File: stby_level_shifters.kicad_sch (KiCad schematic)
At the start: 3 parts, among them U23 NTS0104_DHVQFN

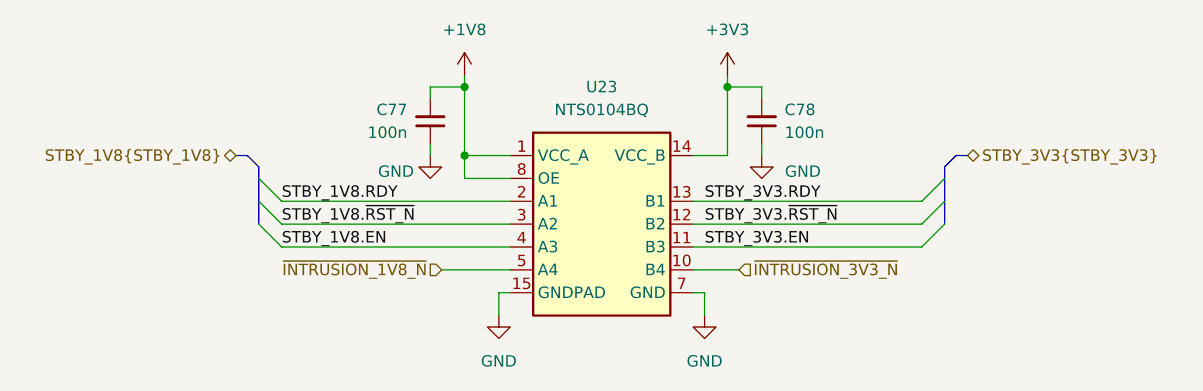
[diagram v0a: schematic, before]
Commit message: [#83148] Connect the level shifters, change STBY bus to individual signals
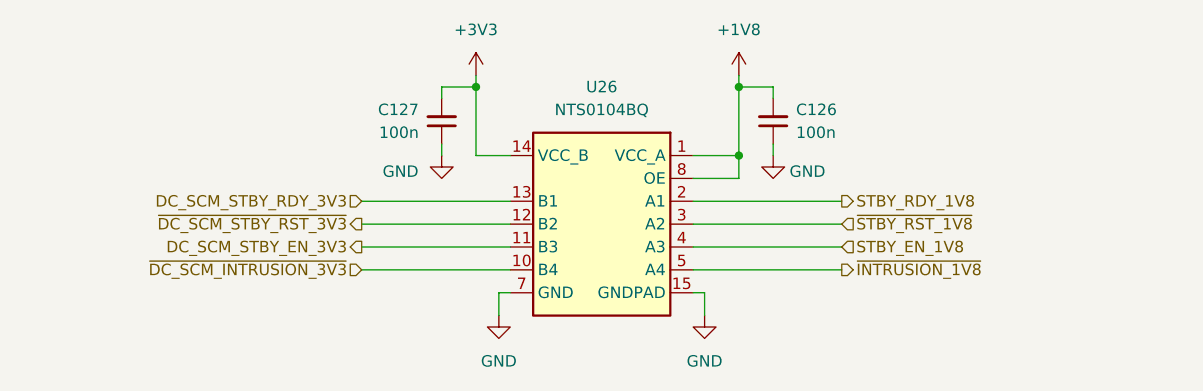
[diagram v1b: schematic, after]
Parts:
- renumbered C77 to C126, C78 to C127, U23 to U26
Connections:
- net STBY_1V8.EN renamed STBY_EN_1V8
- net STBY_1V8.RDY renamed STBY_RDY_1V8
- net STBY_1V8.~{RST_N} renamed ~{STBY_RST_1V8}
- net STBY_3V3.EN renamed DC_SCM_STBY_EN_3V3
- net STBY_3V3.RDY renamed DC_SCM_STBY_RDY_3V3
- net STBY_3V3.~{RST_N} renamed ~{DC_SCM_STBY_RST_3V3}
- net ~{INTRUSION_1V8_N} renamed ~{INTRUSION_1V8}
- net ~{INTRUSION_3V3_N} renamed ~{DC_SCM_INTRUSION_3V3}
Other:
- moved on the sheet: C126, C127

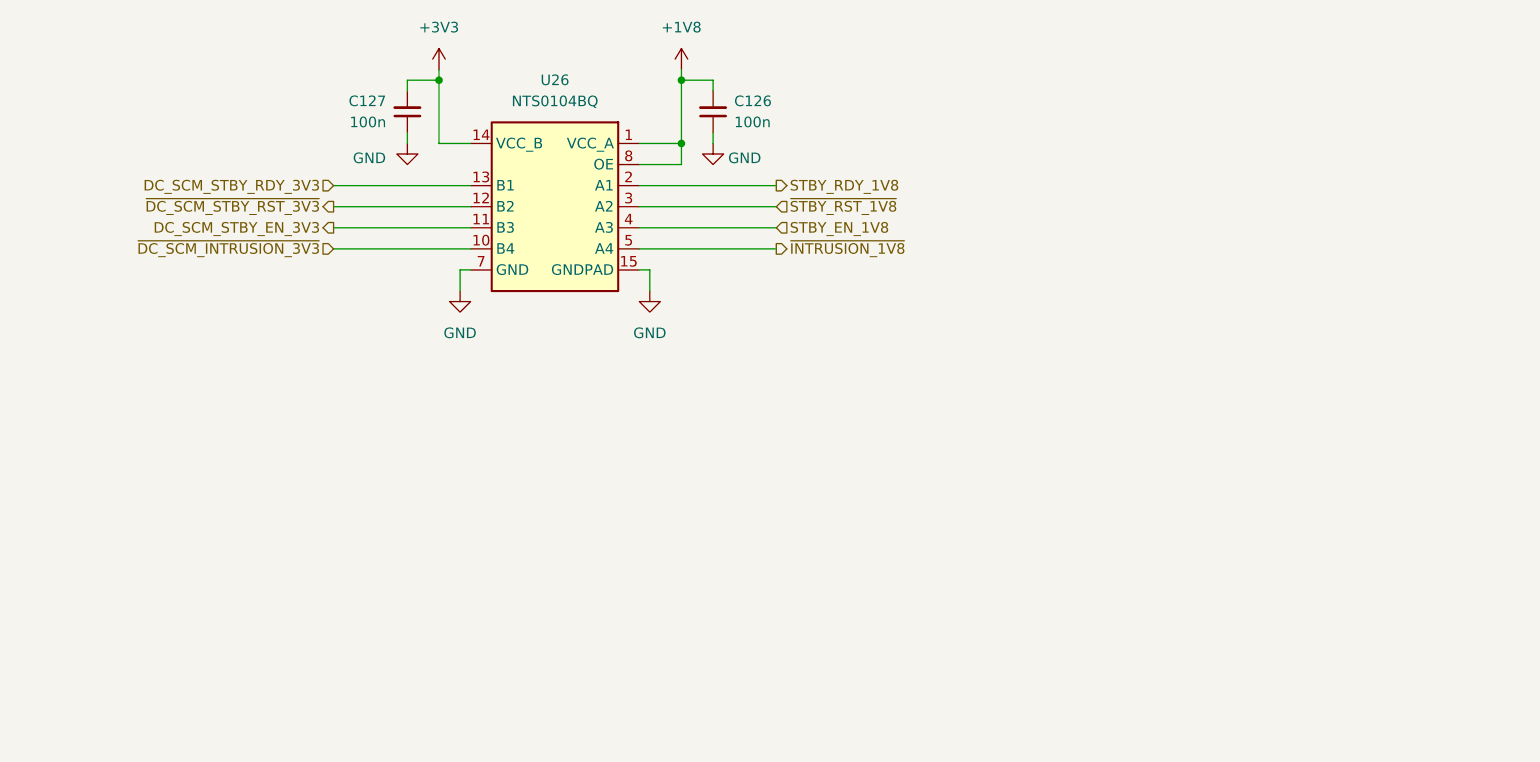
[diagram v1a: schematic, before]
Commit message: Changed A4 sheets to A3 and cleaned them up
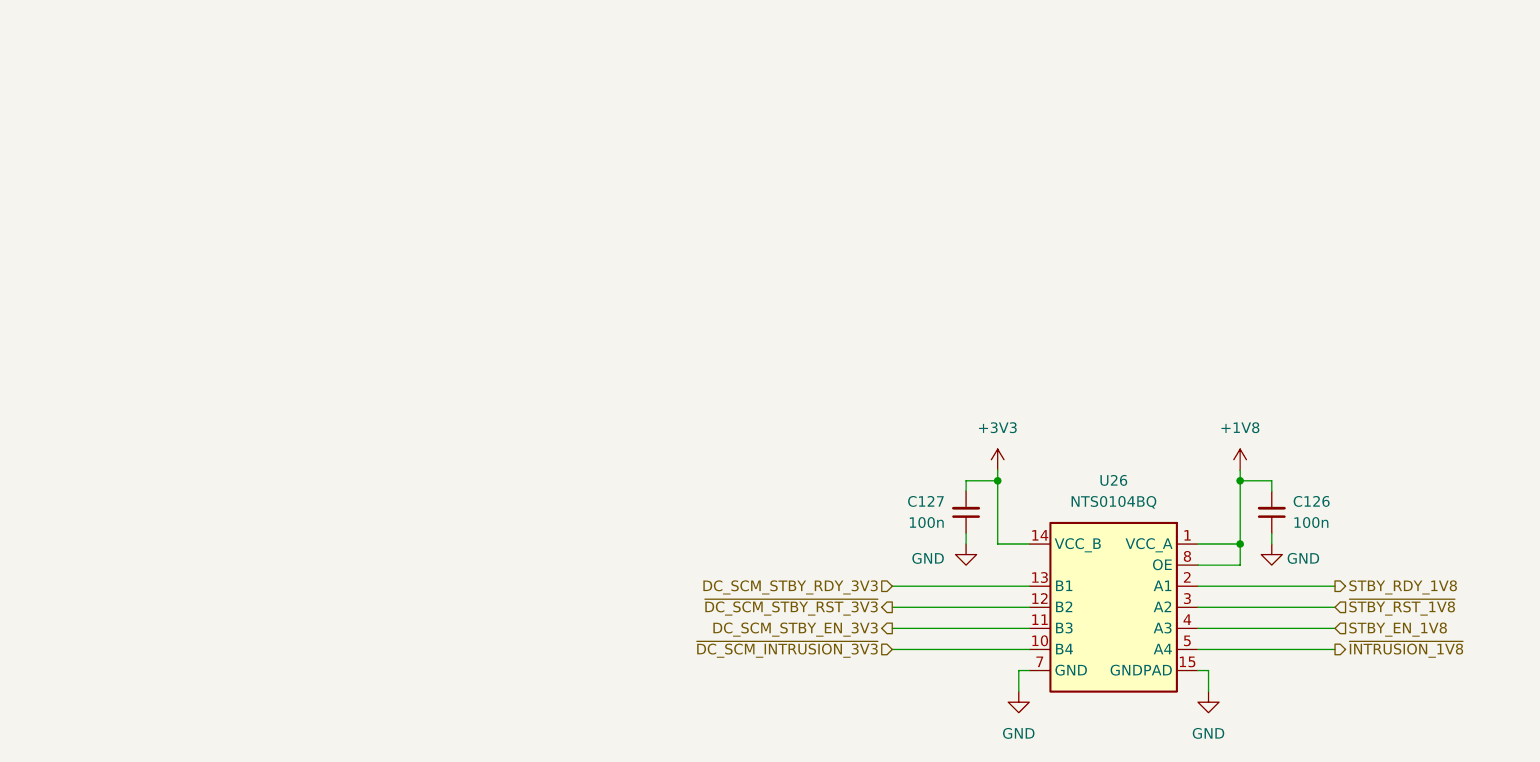
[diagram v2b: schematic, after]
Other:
- title: (none) -> BMC Reference Carrier Board
- moved on the sheet: C126, C127, U26

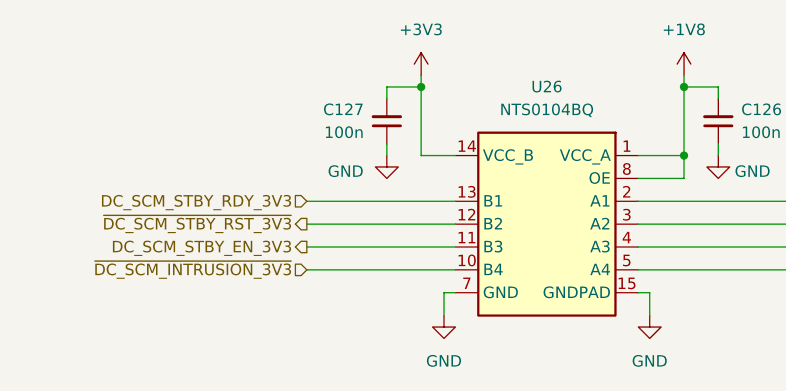
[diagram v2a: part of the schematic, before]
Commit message: [#83362] Fix connections of headers, add I2C mux
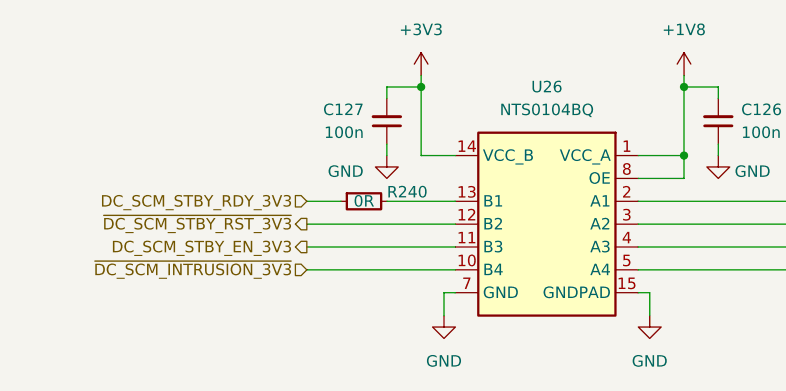
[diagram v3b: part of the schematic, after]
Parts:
- added R240: R_0R_0402, antmicro-footprints:R_0402_1005Metric, symbol antmicroResistors0402:R_0R_0402
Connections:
- net DC_SCM_STBY_RDY_3V3: now also R240.1; no longer U26.13 (B1)
- new net: R240.2, U26.13 (B1)
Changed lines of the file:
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@@
 	(wire
 		(pts
-			(xy 190.5 144.78) (xy 207.01 144.78)
+			(xy 190.5 144.78) (xy 194.31 144.78)
+		)
+		(stroke
+			(width 0)
+			(type default)
+		)
+	)
+	(wire
+		(pts
+			(xy 199.39 144.78) (xy 207.01 144.78)
 		)
 		(stroke
@@
 					(unit 1)
 				)
+			)
+		)
+	)
+	(symbol
+		(lib_id "antmicroResistors0402:R_0R_0402")
+		(at 194.31 144.78 0)
+		(unit 1)
+		(exclude_from_sim no)
+		(in_bom yes)
+		(on_board yes)
+		(dnp no)
+		(property "Reference" "R240"
+			(at 199.39 143.764 0)
+			(effects
+				(font
+					(size 1.27 1.27)
+					(thickness 0.15)
+				)
+				(justify left)
+			)
+		)
+		(property "Value" "R_0R_0402"
+			(at 214.63 157.48 0)
+			(effects
+				(font
+					(size 1.27 1.27)
+					(thickness 0.15)
+				)
+				(justify left bottom)
+				(hide yes)
+			)
+		)
+		(property "Footprint" "antmicro-footprints:R_0402_1005Metric"
+			(at 214.63 160.02 0)
+			(effects
+				(font
+					(size 1.27 1.27)
+					(thickness 0.15)
+				)
+				(justify left bottom)
+				(hide yes)
+			)
+		)
+		(property "Datasheet" "https://industrial.panasonic.com/cdbs/www-data/pdf/RDA0000/AOA0000C301.pdf"
+			(at 214.63 162.56 0)
+			(effects
+				(font
+					(size 1.27 1.27)
+					(thickness 0.15)
+				)
+				(justify left bottom)
+				(hide yes)
+			)
+		)
+		(property "Description" "SMD Chip Resistor, Jumper, 0 ohm, 100 mW, 0402 [1005 Metric], Thick Film, General Purpose"
+			(at 194.31 144.78 0)
+			(effects
+				(font
+					(size 1.27 1.27)
+				)
+				(hide yes)
+			)
+		)
+		(property "MPN" "ERJ2GE0R00X"
+			(at 214.63 165.1 0)
+			(effects
+				(font
+					(size 1.27 1.27)
+					(thickness 0.15)
+				)
+				(justify left bottom)
+				(hide yes)
+			)
+		)
+		(property "Manufacturer" "Panasonic"
+			(at 214.63 167.64 0)
+			(effects
+				(font
+					(size 1.27 1.27)
+					(thickness 0.15)
+				)
+				(justify left bottom)
+				(hide yes)
+			)
+		)
+		(property "License" "Apache-2.0"
+			(at 214.63 170.18 0)
+			(effects
+				(font
+					(size 1.27 1.27)
+					(thickness 0.15)
+				)
+				(justify left bottom)
+				(hide yes)
+			)
+		)
+		(property "Author" "Antmicro"
+			(at 214.63 172.72 0)
+			(effects
+				(font
+					(size 1.27 1.27)
+					(thickness 0.15)
+				)
+				(justify left bottom)
+				(hide yes)
+			)
+		)
+		(property "Val" "0R"
+			(at 196.85 144.78 0)
+			(effects
+				(font
+					(size 1.27 1.27)
+					(thickness 0.15)
+				)
+			)
+		)
+		(property "Tolerance" "~"
+			(at 214.63 154.94 0)
+			(effects
+				(font
+					(size 1.27 1.27)
+				)
+				(justify left bottom)
+				(hide yes)
+			)
+		)
+		(property "Current" "1A"
+			(at 214.63 175.26 0)
+			(effects
+				(font
+					(size 1.27 1.27)
+					(thickness 0.15)
+				)
+				(justify left bottom)
+				(hide yes)
+			)
+		)
+		(pin "1"
+		)
+		(pin "2"
+		)
+		(instances
+			(project "bmc-reference-carrier-board"
+				(path "/5f636c45-3c15-4731-8931-4625e0dab7e4/40b8b518-c83d-44f5-8ab2-da7ec61f9cc6"
+					(reference "R240")
+					(unit 1)
+				)

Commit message: [#83609] Reannotate board
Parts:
- renumbered C127 to C164, C126 to C165, R240 to R287, U26 to U34
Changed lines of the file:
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@@
 		(dnp no)
 		(fields_autoplaced yes)
-		(property "Reference" "#PWR0158"
+		(property "Reference" "#PWR0321"
 			(at 214.63 160.02 0)
 			(effects
@@
 			(project "bmc-reference-carrier-board"
 				(path "/5f636c45-3c15-4731-8931-4625e0dab7e4/40b8b518-c83d-44f5-8ab2-da7ec61f9cc6"
-					(reference "#PWR0158")
+					(reference "#PWR0321")
 					(unit 1)
 				)
@@
 		(on_board yes)
 		(dnp no)
-		(property "Reference" "#PWR0155"
+		(property "Reference" "#PWR0324"
 			(at 245.11 142.24 0)
 			(effects
@@
 			(project "bmc-reference-carrier-board"
 				(path "/5f636c45-3c15-4731-8931-4625e0dab7e4/40b8b518-c83d-44f5-8ab2-da7ec61f9cc6"
-					(reference "#PWR0155")
+					(reference "#PWR0324")
 					(unit 1)
 				)
@@
 		(dnp no)
 		(fields_autoplaced yes)
-		(property "Reference" "C127"
+		(property "Reference" "C164"
 			(at 196.85 134.6136 90)
 			(effects
@@
 			(project "bmc-reference-carrier-board"
 				(path "/5f636c45-3c15-4731-8931-4625e0dab7e4/40b8b518-c83d-44f5-8ab2-da7ec61f9cc6"
-					(reference "C127")
+					(reference "C164")
 					(unit 1)
 				)
@@
 		(on_board yes)
 		(dnp no)
-		(property "Reference" "C126"
+		(property "Reference" "C165"
 			(at 238.76 134.6136 90)
 			(effects
@@
 			(project "bmc-reference-carrier-board"
 				(path "/5f636c45-3c15-4731-8931-4625e0dab7e4/40b8b518-c83d-44f5-8ab2-da7ec61f9cc6"
-					(reference "C126")
+					(reference "C165")
 					(unit 1)
 				)
@@
 		(dnp no)
 		(fields_autoplaced yes)
-		(property "Reference" "#PWR0157"
+		(property "Reference" "#PWR0322"
 			(at 237.49 160.02 0)
 			(effects
@@
 			(project "bmc-reference-carrier-board"
 				(path "/5f636c45-3c15-4731-8931-4625e0dab7e4/40b8b518-c83d-44f5-8ab2-da7ec61f9cc6"
-					(reference "#PWR0157")
+					(reference "#PWR0322")
 					(unit 1)
 				)
@@
 		(dnp no)
 		(fields_autoplaced yes)
-		(property "Reference" "#PWR0154"
+		(property "Reference" "#PWR0320"
 			(at 187.96 130.81 0)
 			(effects
@@
 			(project "bmc-reference-carrier-board"
 				(path "/5f636c45-3c15-4731-8931-4625e0dab7e4/40b8b518-c83d-44f5-8ab2-da7ec61f9cc6"
-					(reference "#PWR0154")
+					(reference "#PWR0320")
 					(unit 1)
 				)
@@
 		(dnp no)
 		(fields_autoplaced yes)
-		(property "Reference" "#PWR0153"
+		(property "Reference" "#PWR0323"
 			(at 217.17 133.35 0)
 			(effects
@@
 			(project "bmc-reference-carrier-board"
 				(path "/5f636c45-3c15-4731-8931-4625e0dab7e4/40b8b518-c83d-44f5-8ab2-da7ec61f9cc6"
-					(reference "#PWR0153")
+					(reference "#PWR0323")
 					(unit 1)
 				)
@@
 		(dnp no)
 		(fields_autoplaced yes)
-		(property "Reference" "U26"
+		(property "Reference" "U34"
 			(at 217.17 132.08 0)
 			(effects
@@
 			(project "bmc-reference-carrier-board"
 				(path "/5f636c45-3c15-4731-8931-4625e0dab7e4/40b8b518-c83d-44f5-8ab2-da7ec61f9cc6"
-					(reference "U26")
+					(reference "U34")
 					(unit 1)
 				)
@@
 		(on_board yes)
 		(dnp no)
-		(property "Reference" "#PWR0156"
+		(property "Reference" "#PWR0319"
 			(at 190.5 142.24 0)
 			(effects
@@
 			(project "bmc-reference-carrier-board"
 				(path "/5f636c45-3c15-4731-8931-4625e0dab7e4/40b8b518-c83d-44f5-8ab2-da7ec61f9cc6"
-					(reference "#PWR0156")
+					(reference "#PWR0319")
 					(unit 1)
 				)
@@
 		(on_board yes)
 		(dnp no)
-		(property "Reference" "R240"
+		(property "Reference" "R287"
 			(at 199.39 143.764 0)
 			(effects
@@
 			(project "bmc-reference-carrier-board"
 				(path "/5f636c45-3c15-4731-8931-4625e0dab7e4/40b8b518-c83d-44f5-8ab2-da7ec61f9cc6"
-					(reference "R240")
+					(reference "R287")
 					(unit 1)
 				)
